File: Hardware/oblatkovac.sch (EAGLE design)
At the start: 40 parts, among them SW1 EC12E_SW, T1 2N2222, X1 ~230V

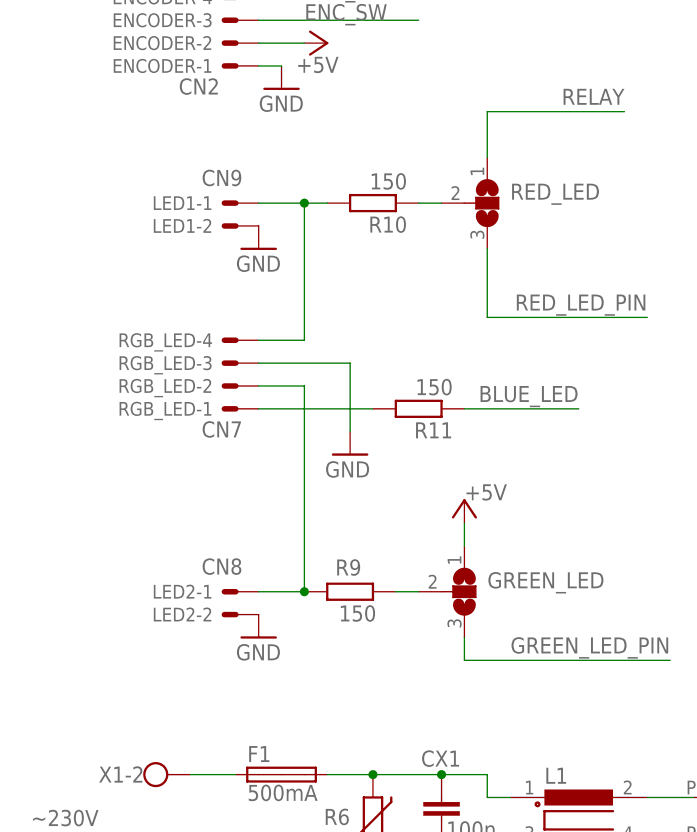
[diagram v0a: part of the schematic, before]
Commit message: - Improved temperature sensing, heater control, and UI. - Integrated EEPROM for saving settings. - Configured button handlers for menu navigation and start/stop functionality. - Established pin definitions for various components including relay, buzzer, and LEDs. - Updated README.md files - Reorganized folder structure - Added 3D models
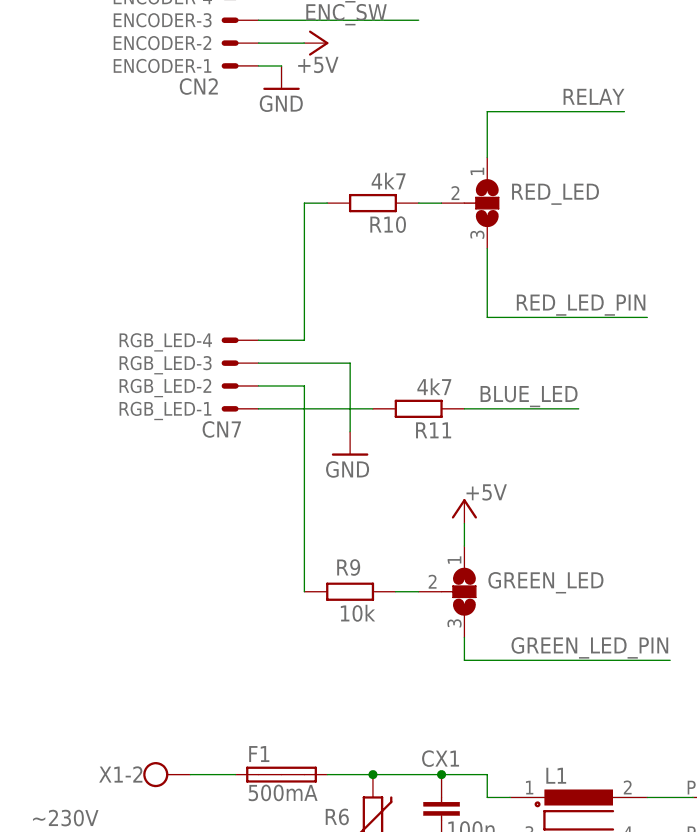
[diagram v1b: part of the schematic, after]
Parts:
- removed LED1: CN9, Rembrandt Electronics - JST XH Connectors v1-0:JST-XH-02-PIN-LONG-PAD
- removed LED2: CN8, Rembrandt Electronics - JST XH Connectors v1-0:JST-XH-02-PIN-LONG-PAD
- R10, R11: value 150 -> 4k7
- R9: value 150 -> 10k
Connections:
- net GND: no longer LED1-2.S, LED2-2.S
- net N$5: no longer LED2-1.S
- net N$6: no longer LED1-1.S
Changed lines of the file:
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@@
 <part name="P+9" library="supply1" library_urn="urn:adsk.eagle:library:371" deviceset="+5V" device=""/>
 <part name="C4" library="rcl" library_urn="urn:adsk.eagle:library:334" deviceset="C-EU" device="050-024X044" package3d_urn="urn:adsk.eagle:package:23643/1" value="100nF"/>
-<part name="LED1" library="Rembrandt Electronics - JST XH Connectors v1-0" deviceset="JST-XH-02-PIN" device="-LONG-PAD" value="CN9"/>
-<part name="LED2" library="Rembrandt Electronics - JST XH Connectors v1-0" deviceset="JST-XH-02-PIN" device="-LONG-PAD" value="CN8"/>
-<part name="GND13" library="supply1" library_urn="urn:adsk.eagle:library:371" deviceset="GND" device=""/>
-<part name="R9" library="rcl" library_urn="urn:adsk.eagle:library:334" deviceset="R-EU_" device="0207/10" package3d_urn="urn:adsk.eagle:package:23491/2" value="150"/>
+<part name="R9" library="rcl" library_urn="urn:adsk.eagle:library:334" deviceset="R-EU_" device="0207/10" package3d_urn="urn:adsk.eagle:package:23491/2" value="10k"/>
 <part name="P+10" library="supply1" library_urn="urn:adsk.eagle:library:371" deviceset="+5V" device=""/>
-<part name="R10" library="rcl" library_urn="urn:adsk.eagle:library:334" deviceset="R-EU_" device="0207/10" package3d_urn="urn:adsk.eagle:package:23491/2" value="150"/>
-<part name="GND14" library="supply1" library_urn="urn:adsk.eagle:library:371" deviceset="GND" device=""/>
+<part name="R10" library="rcl" library_urn="urn:adsk.eagle:library:334" deviceset="R-EU_" device="0207/10" package3d_urn="urn:adsk.eagle:package:23491/2" value="4k7"/>
 <part name="OLED_PIN2" library="jumper" library_urn="urn:adsk.eagle:library:252" deviceset="SJ2W" device="" package3d_urn="urn:adsk.eagle:package:15474/1"/>
 <part name="OLED_PIN1" library="jumper" library_urn="urn:adsk.eagle:library:252" deviceset="SJ2W" device="" package3d_urn="urn:adsk.eagle:package:15474/1"/>
@@
 <part name="RGB_LED" library="Rembrandt Electronics - JST XH Connectors v1-0" deviceset="JST-XH-04-PIN" device="-LONG-PAD" value="CN7"/>
 <part name="GND18" library="supply1" library_urn="urn:adsk.eagle:library:371" deviceset="GND" device=""/>
-<part name="R11" library="rcl" library_urn="urn:adsk.eagle:library:334" deviceset="R-EU_" device="0207/10" package3d_urn="urn:adsk.eagle:package:23491/2" value="150"/>
+<part name="R11" library="rcl" library_urn="urn:adsk.eagle:library:334" deviceset="R-EU_" device="0207/10" package3d_urn="urn:adsk.eagle:package:23491/2" value="4k7"/>
 <part name="GREEN_LED" library="jumper" library_urn="urn:adsk.eagle:library:252" deviceset="SJ2W" device="" package3d_urn="urn:adsk.eagle:package:15474/1"/>
 <part name="GND19" library="supply1" library_urn="urn:adsk.eagle:library:371" deviceset="GND" device=""/>
@@
 <attribute name="VALUE" x="120.65" y="28.067" size="1.778" layer="96" rot="R180"/>
 </instance>
-<instance part="LED1" gate="-2" x="30.48" y="88.9" smashed="yes" rot="R180">
-<attribute name="NAME" x="27.94" y="89.662" size="1.524" layer="95" rot="R180"/>
-</instance>
-<instance part="LED1" gate="-1" x="30.48" y="91.44" smashed="yes" rot="R180">
-<attribute name="NAME" x="27.94" y="92.202" size="1.524" layer="95" rot="R180"/>
-<attribute name="VALUE" x="31.242" y="95.123" size="1.778" layer="96" rot="R180"/>
-</instance>
-<instance part="LED2" gate="-2" x="30.48" y="45.72" smashed="yes" rot="R180">
-<attribute name="NAME" x="27.94" y="46.482" size="1.524" layer="95" rot="R180"/>
-</instance>
-<instance part="LED2" gate="-1" x="30.48" y="48.26" smashed="yes" rot="R180">
-<attribute name="NAME" x="27.94" y="49.022" size="1.524" layer="95" rot="R180"/>
-<attribute name="VALUE" x="31.242" y="51.943" size="1.778" layer="96" rot="R180"/>
-</instance>
-<instance part="GND13" gate="1" x="33.02" y="43.18" smashed="yes">
-<attribute name="VALUE" x="30.48" y="40.64" size="1.778" layer="96"/>
-</instance>
 <instance part="R9" gate="G$1" x="43.18" y="48.26" smashed="yes">
 <attribute name="NAME" x="44.45" y="51.8414" size="1.778" layer="95" rot="R180"/>
@@
 <attribute name="NAME" x="49.53" y="89.9414" size="1.778" layer="95" rot="R180"/>
 <attribute name="VALUE" x="49.53" y="94.742" size="1.778" layer="96" rot="R180"/>
-</instance>
-<instance part="GND14" gate="1" x="33.02" y="86.36" smashed="yes">
-<attribute name="VALUE" x="30.48" y="83.82" size="1.778" layer="96"/>
 </instance>
 <instance part="OLED_PIN2" gate="G$1" x="218.44" y="121.92" smashed="yes">
@@
 <net name="N$5" class="0">
 <segment>
-<pinref part="LED2" gate="-1" pin="S"/>
 <pinref part="R9" gate="G$1" pin="1"/>
-<wire x1="38.1" y1="48.26" x2="33.02" y2="48.26" width="0.1524" layer="91"/>
 <pinref part="RGB_LED" gate="-2" pin="S"/>
 <wire x1="33.02" y1="71.12" x2="38.1" y2="71.12" width="0.1524" layer="91"/>
 <wire x1="38.1" y1="71.12" x2="38.1" y2="48.26" width="0.1524" layer="91"/>
-<junction x="38.1" y="48.26"/>
 </segment>
 </net>
 <net name="N$6" class="0">
 <segment>
-<pinref part="LED1" gate="-1" pin="S"/>
 <pinref part="R10" gate="G$1" pin="2"/>
 <wire x1="40.64" y1="91.44" x2="38.1" y2="91.44" width="0.1524" layer="91"/>
 <pinref part="RGB_LED" gate="-4" pin="S"/>
-<wire x1="38.1" y1="91.44" x2="33.02" y2="91.44" width="0.1524" layer="91"/>
 <wire x1="33.02" y1="76.2" x2="38.1" y2="76.2" width="0.1524" layer="91"/>
 <wire x1="38.1" y1="76.2" x2="38.1" y2="91.44" width="0.1524" layer="91"/>
-<junction x="38.1" y="91.44"/>
 </segment>
 </net>
@@
 </segment>
 <segment>
-<pinref part="LED2" gate="-2" pin="S"/>
-<pinref part="GND13" gate="1" pin="GND"/>
-</segment>
-<segment>
-<pinref part="LED1" gate="-2" pin="S"/>
-<pinref part="GND14" gate="1" pin="GND"/>
-</segment>
-<segment>
